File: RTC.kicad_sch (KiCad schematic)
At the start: 5 parts, among them U201 DS1307ZN+, X201 ASE-xxxMHz

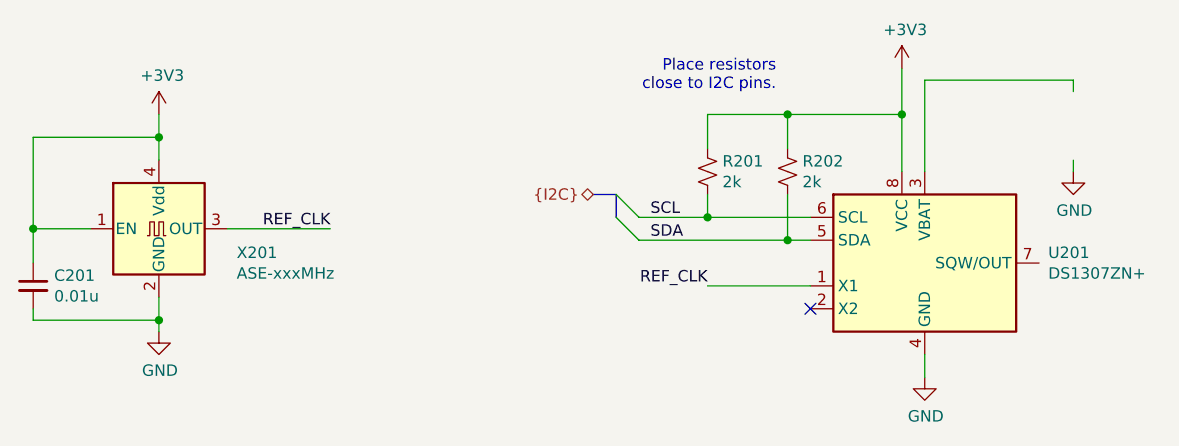
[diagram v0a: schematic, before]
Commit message: Attach ethernet to PL, layout and route
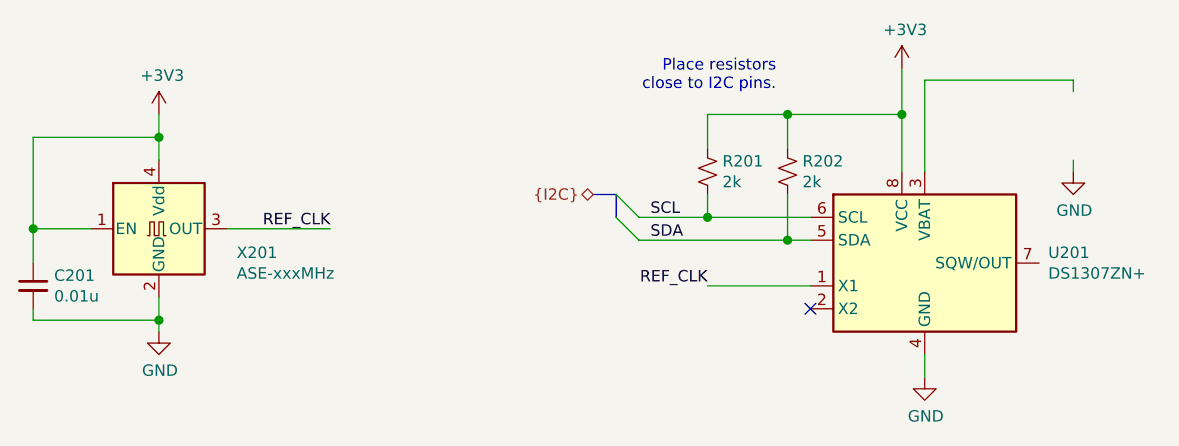
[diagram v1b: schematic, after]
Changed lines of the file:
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@@
-(kicad_sch (version 20200714) (host eeschema "5.99.0-unknown-bf445c1~102~ubuntu20.04.1")
-  (page 1 15)
+(kicad_sch (version 20200714) (host eeschema "5.99.0-unknown-a146cd9~102~ubuntu20.04.1")
+  (page 2 15)
   (paper "B")
   (title_block
@@
     (comment 1 "Drawn by: Cameron McQuinn")
   )
-  (junction (at 116.84 114.3) (diameter 0) (color 0 0 0 0))
-  (junction (at 130.81 104.14) (diameter 0) (color 0 0 0 0))
-  (junction (at 130.81 124.46) (diameter 0) (color 0 0 0 0))
-  (junction (at 191.77 113.03) (diameter 0) (color 0 0 0 0))
-  (junction (at 200.66 101.6) (diameter 0) (color 0 0 0 0))
-  (junction (at 200.66 115.57) (diameter 0) (color 0 0 0 0))
-  (junction (at 213.36 101.6) (diameter 0) (color 0 0 0 0))
+  (junction (at 116.84 114.3) (diameter 1.016) (color 0 0 0 0))
+  (junction (at 130.81 104.14) (diameter 1.016) (color 0 0 0 0))
+  (junction (at 130.81 124.46) (diameter 1.016) (color 0 0 0 0))
+  (junction (at 191.77 113.03) (diameter 1.016) (color 0 0 0 0))
+  (junction (at 200.66 101.6) (diameter 1.016) (color 0 0 0 0))
+  (junction (at 200.66 115.57) (diameter 1.016) (color 0 0 0 0))
+  (junction (at 213.36 101.6) (diameter 1.016) (color 0 0 0 0))
   (no_connect (at 203.2 123.19))
   (bus_entry (at 181.61 110.49) (size 2.54 2.54)
